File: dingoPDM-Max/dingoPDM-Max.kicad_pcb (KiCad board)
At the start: 4 copper layers, 72.4 x 95.2 mm, 136 parts, among them J1 RedCubeTerminal, J2 USB_C_Receptacle_USB2.0, J3 RedCubeTerminal, J4 Conn_01x12, J5 TC, SW1 BOOT, U1 VXO780x-500-M, U10 BTS70015-1ESP, U11 BTS70015-1ESP, U2 LD1117S33CTR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

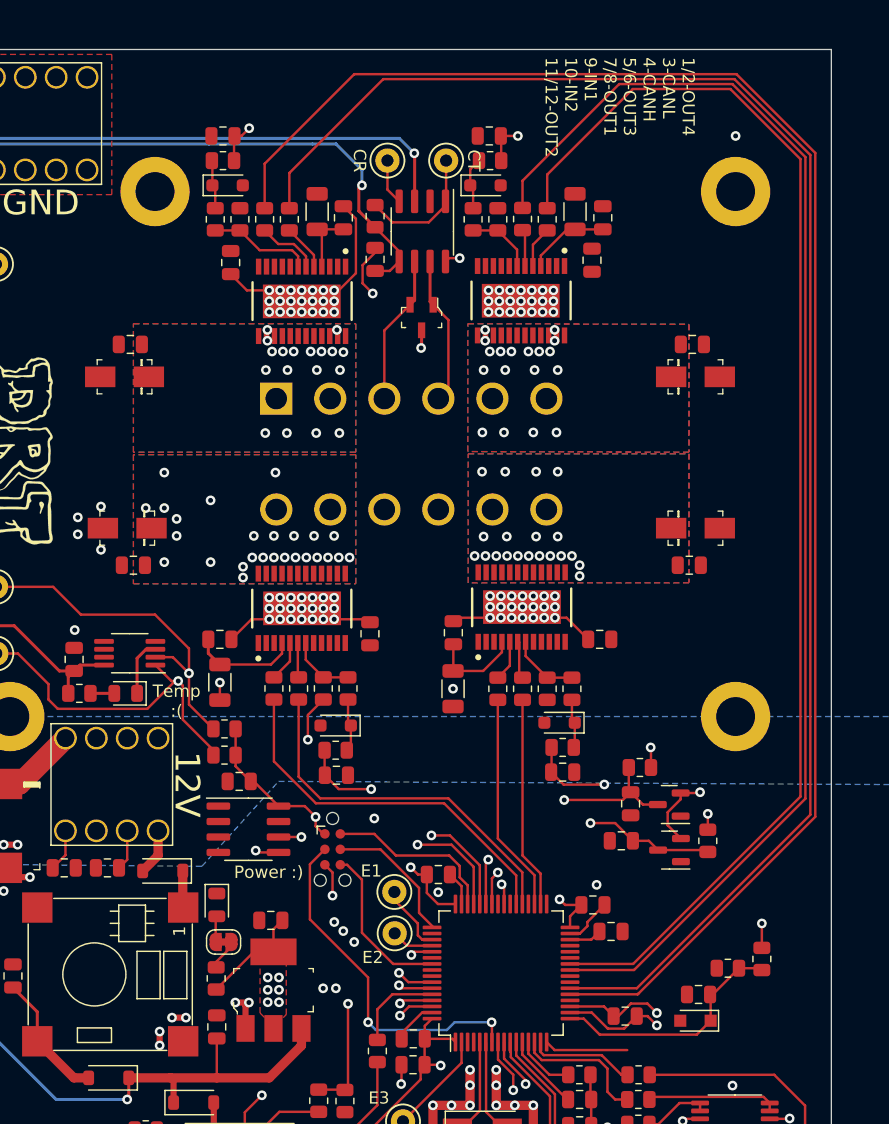
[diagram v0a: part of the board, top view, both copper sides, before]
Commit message: First layout complete
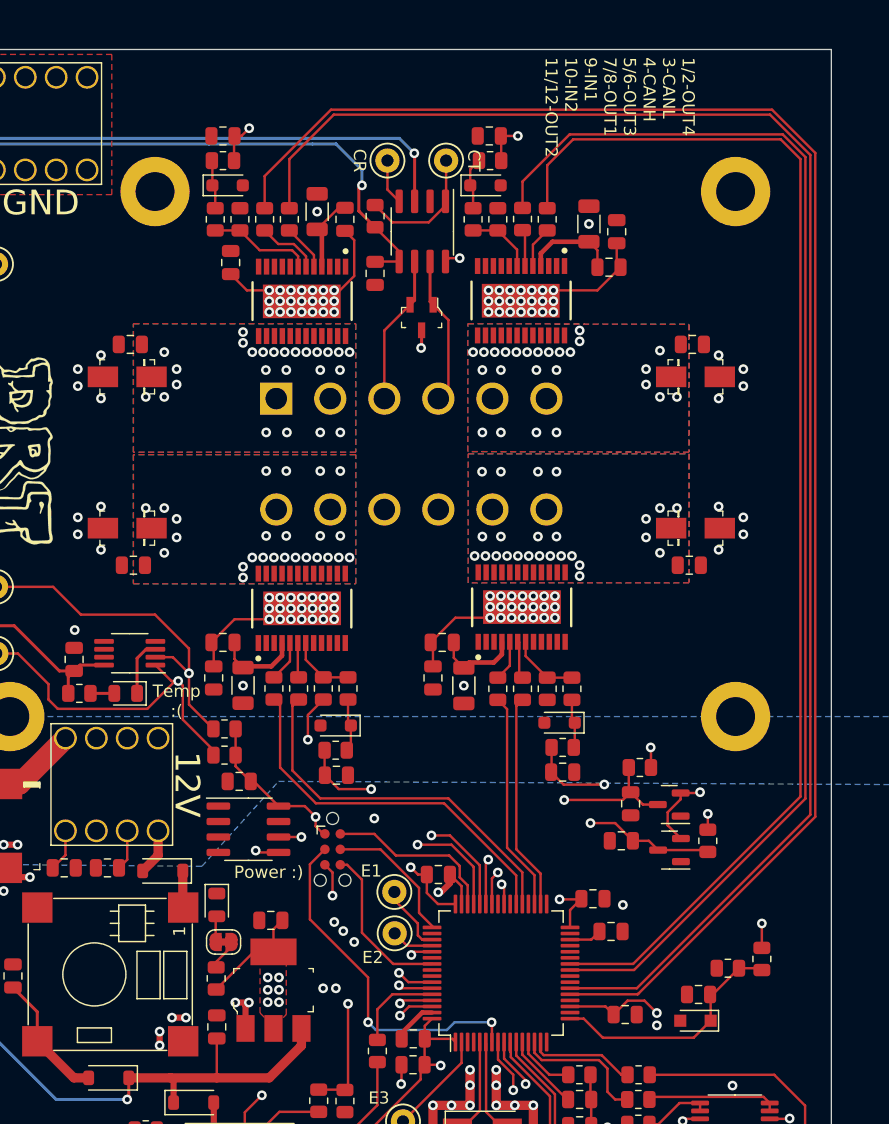
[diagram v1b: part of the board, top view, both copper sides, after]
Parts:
- moved C24 14.1 mm to (1.78, 18.4), turned to 90 degrees
- moved C28 13.4 mm to (-16.3, 18.4)
- moved C31 4.10 mm to (16.3, -15.4), turned to 0 degrees
- moved C32 3.10 mm to (16.9, -18.3)
- moved R30 1.92 mm to (-13.8, 19.0)
- moved R36 1.53 mm to (14.6, -18.9)
- moved C23 1.21 mm to (2.54, 15.5), turned to 180 degrees
- moved C9 1.15 mm to (-2.98, -14.9), turned to -90 degrees
- moved R24 0.92 mm to (4.32, 19.1)
- moved C12 0.51 mm to (14.9, 36.6)
- moved C27 0.36 mm to (-15.5, 15.5), turned to 180 degrees
- moved D19 0.22 mm to (-23.4, -6.35)
- moved C35 0.18 mm to (-5.46, -19.3), turned to -90 degrees
- moved C11 0.13 mm to (17.6, 46.1)
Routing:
- net GND: track 91.6 -> 75.2 mm, vias 51 -> 63
- net +12V: track 79.6 -> 87.8 mm
- net unconnected-(U4-PA2-Pad16): track 6.90 -> 0.00 mm
- net PF_DEN3: track 109.2 -> 105.8 mm
- net PF_DEN4: track 135.5 -> 132.5 mm
- net PF_IN3: track 106.0 -> 103.0 mm
- net Net-(U9-GND): track 8.83 -> 7.01 mm
- net PF_IN4: track 131.5 -> 129.7 mm
- net /HighCurrentDrivers/sheet5F5A40BA2/IS: track 136.5 -> 135.3 mm
- net Net-(U10-GND): track 6.85 -> 7.77 mm
- net Net-(U11-GND): track 5.38 -> 6.25 mm
- net Net-(U8-GND): track 7.72 -> 7.06 mm
- net /HighCurrentDrivers/sheet5F5A40BA1/IS: track 110.4 -> 109.8 mm
- net /MCU/CAN_TX: track 121.2 -> 121.8 mm
- net PF_OUT4: vias 18 -> 25
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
